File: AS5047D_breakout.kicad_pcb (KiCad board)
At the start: 2 copper layers, 5 parts, among them J1 Conn_01x12_Male, U1 AS5047D

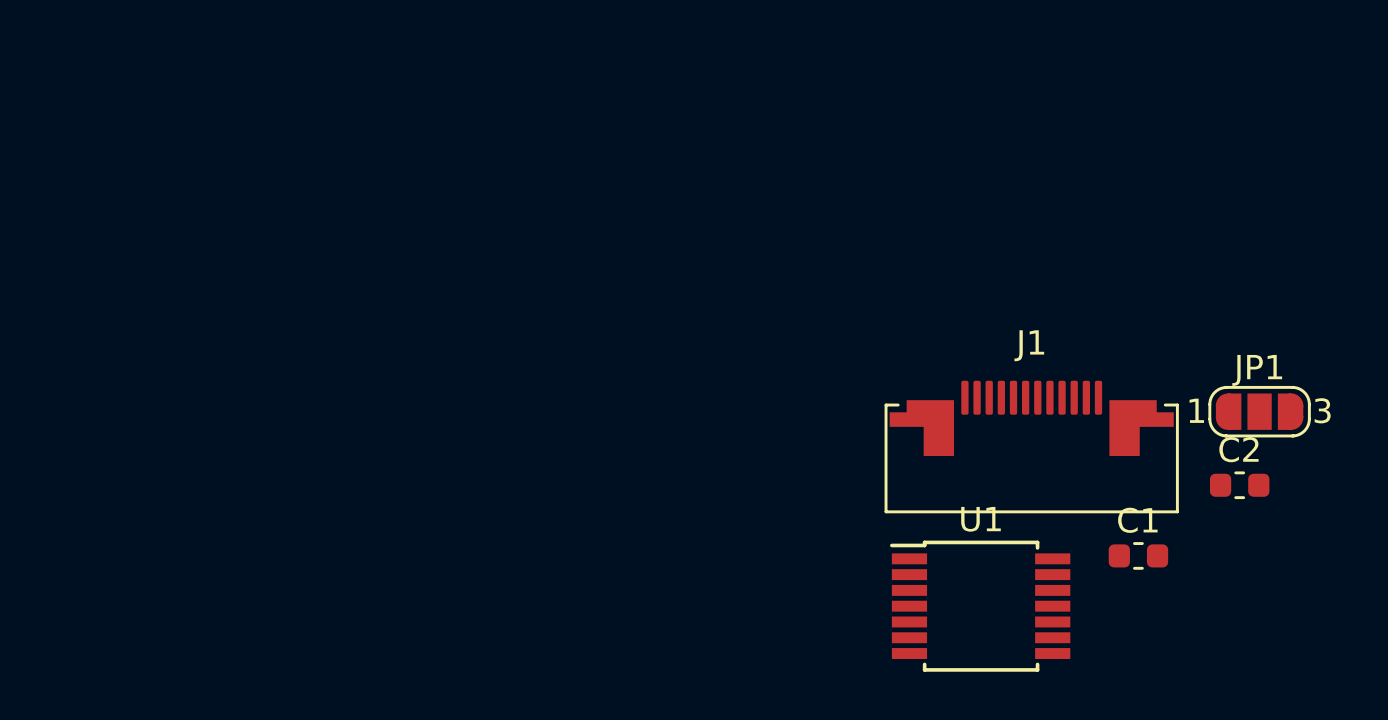
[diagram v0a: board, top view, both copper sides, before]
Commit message: Create encoder breakout board layout
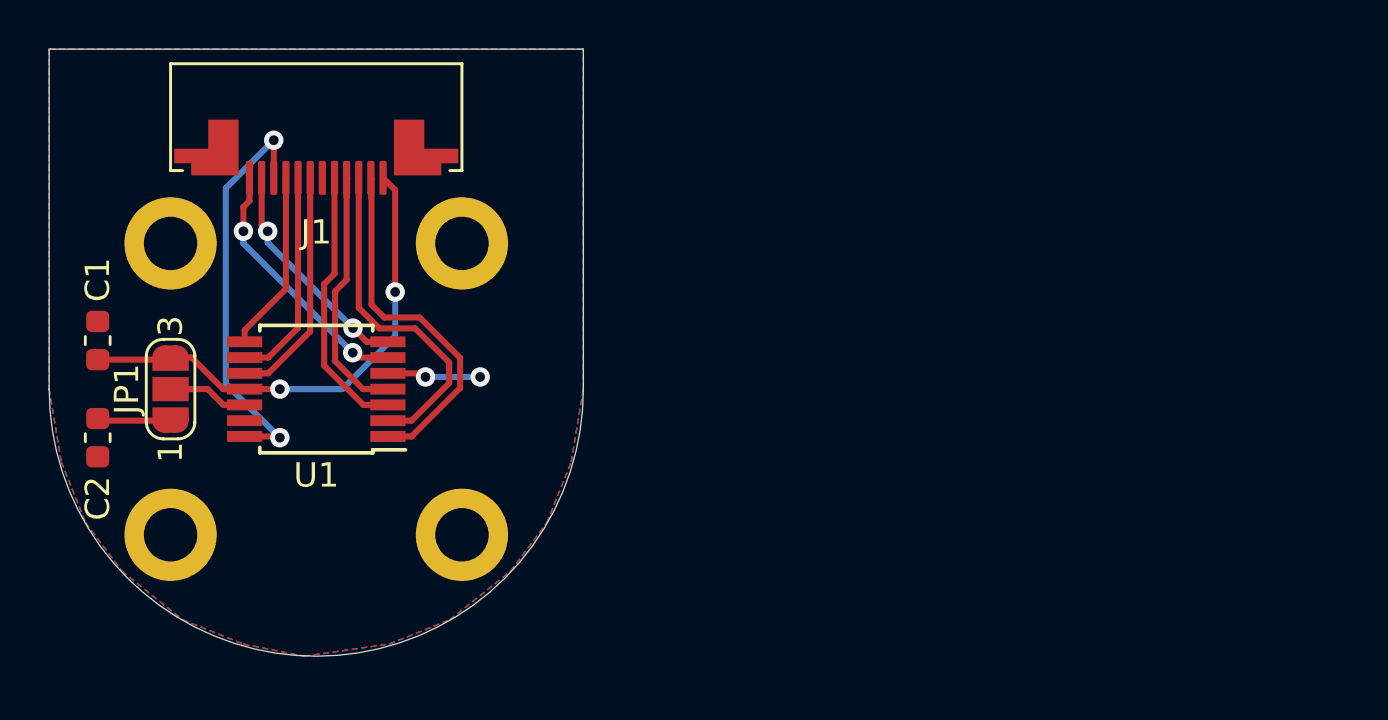
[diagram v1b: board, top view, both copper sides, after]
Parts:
- added G***: LOGO, follow_focus_hw:Gravity_Labs_Logo_Flipped_10mmW, F.Cu at (114.8, 95.8)
- added REF**: MountingHole_2.2mm_M2_DIN965_Pad, MountingHole:MountingHole_2.2mm_M2_DIN965_Pad, F.Cu at (122.0, 102.0)
- added REF**: MountingHole_2.2mm_M2_DIN965_Pad, MountingHole:MountingHole_2.2mm_M2_DIN965_Pad, F.Cu at (110.0, 102.0)
- added REF**: MountingHole_2.2mm_M2_DIN965_Pad, MountingHole:MountingHole_2.2mm_M2_DIN965_Pad, F.Cu at (110.0, 90.0)
- added REF**: MountingHole_2.2mm_M2_DIN965_Pad, MountingHole:MountingHole_2.2mm_M2_DIN965_Pad, F.Cu at (122.0, 90.0)
- moved C2 47.1 mm to (107.0, 98.0), turned to 270 degrees
- moved JP1 44.9 mm to (110.0, 96.0), turned to 90 degrees
- moved C1 43.8 mm to (107.0, 94.0), turned to 90 degrees
- moved J1 31.0 mm to (116.0, 87.0), turned to 180 degrees
- moved U1 28.8 mm to (116.0, 96.0), turned to 180 degrees
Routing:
- net VDD: track 0.00 -> 20.5 mm, vias 0 -> 2
- net /I: track 0.00 -> 17.0 mm, vias 0 -> 2
- net /CSN: track 0.00 -> 15.6 mm
- net /CLK: track 0.00 -> 14.0 mm
- net /MISO: track 0.00 -> 11.2 mm
- net /MOSI: track 0.00 -> 11.2 mm
- net /B: track 0.00 -> 10.7 mm, vias 0 -> 2
- net /U: track 0.00 -> 9.74 mm
- net /A: track 0.00 -> 9.42 mm, vias 0 -> 2
- net /V: track 0.00 -> 8.88 mm
- net /W: track 0.00 -> 7.45 mm
- net GND: track 0.00 -> 3.86 mm, vias 0 -> 2
- net Net-(JP1-Pad2): track 0.00 -> 3.32 mm
- net Net-(C2-Pad1): track 0.00 -> 3.04 mm
- added copper zone on B.Cu, net GND
- added copper zone on F.Cu, net GND
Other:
- board outline added: 22 x 25 mm
- board text added: "Created By: Eduardo Mucino Andrew Chau"

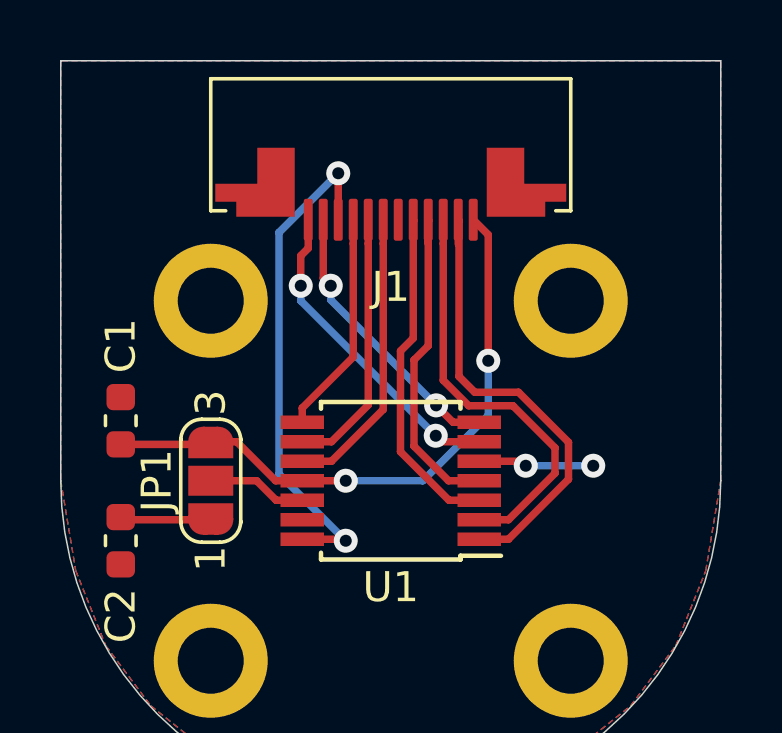
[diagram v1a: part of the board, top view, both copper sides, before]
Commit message: Adjust harness connector location on AS5047D board
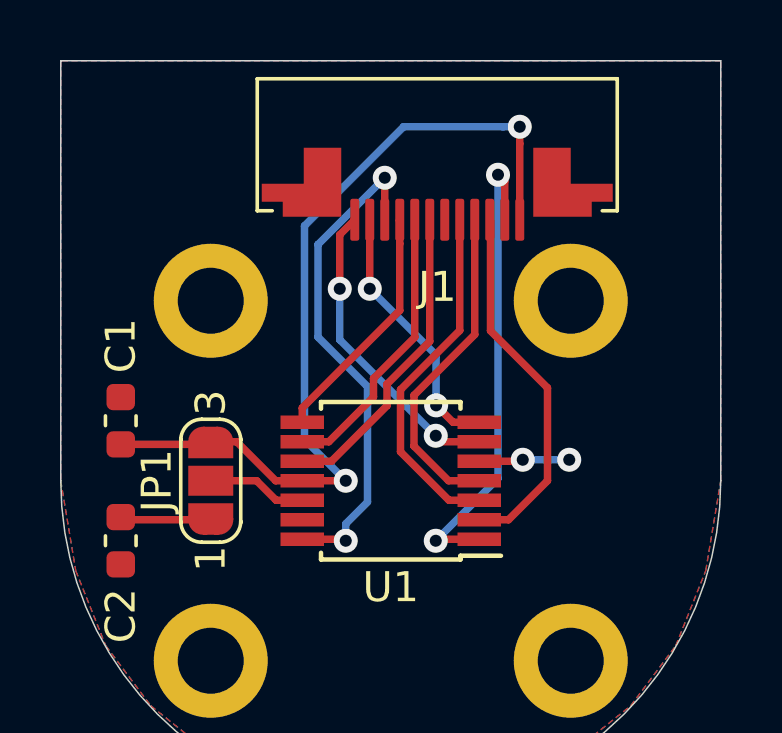
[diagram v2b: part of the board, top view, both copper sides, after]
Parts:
- moved J1 1.55 mm to (117.5, 87.0)
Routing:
- net VDD: track 20.5 -> 28.8 mm
- net /CLK: track 14.0 -> 12.3 mm
- net GND: track 3.86 -> 3.02 mm
- net /W: track 7.45 -> 8.13 mm
- net /A: track 9.42 -> 8.77 mm
- net /U: track 9.74 -> 10.4 mm
- net /MISO: track 11.2 -> 11.8 mm
- net /V: track 8.88 -> 9.47 mm
- net /CSN: track 15.6 -> 16.1 mm, vias 0 -> 2

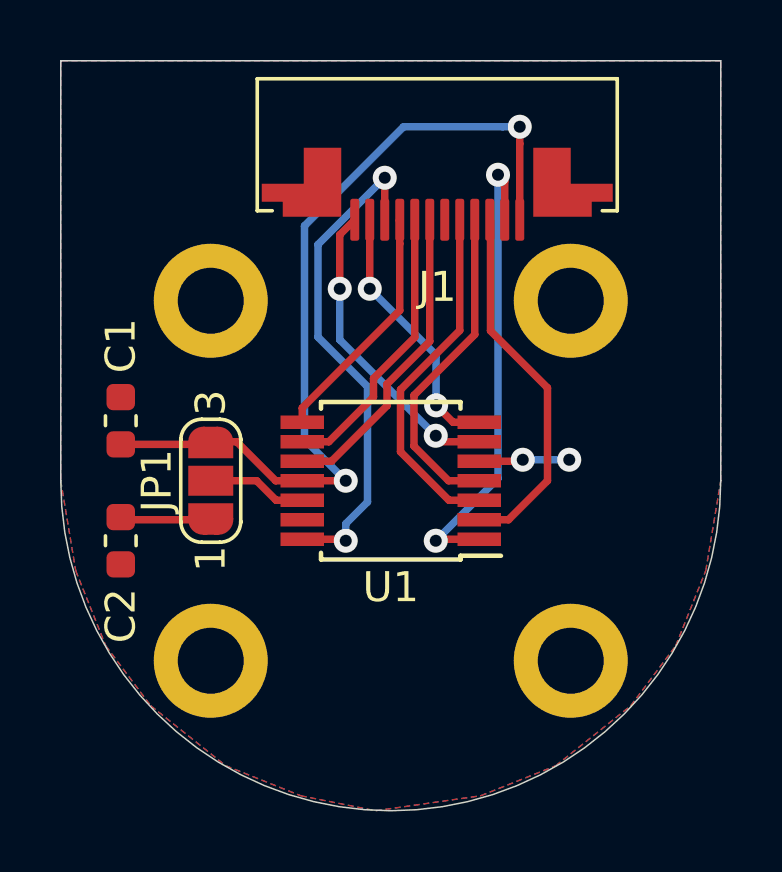
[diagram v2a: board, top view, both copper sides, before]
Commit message: Modify AS5047D breakout form factor
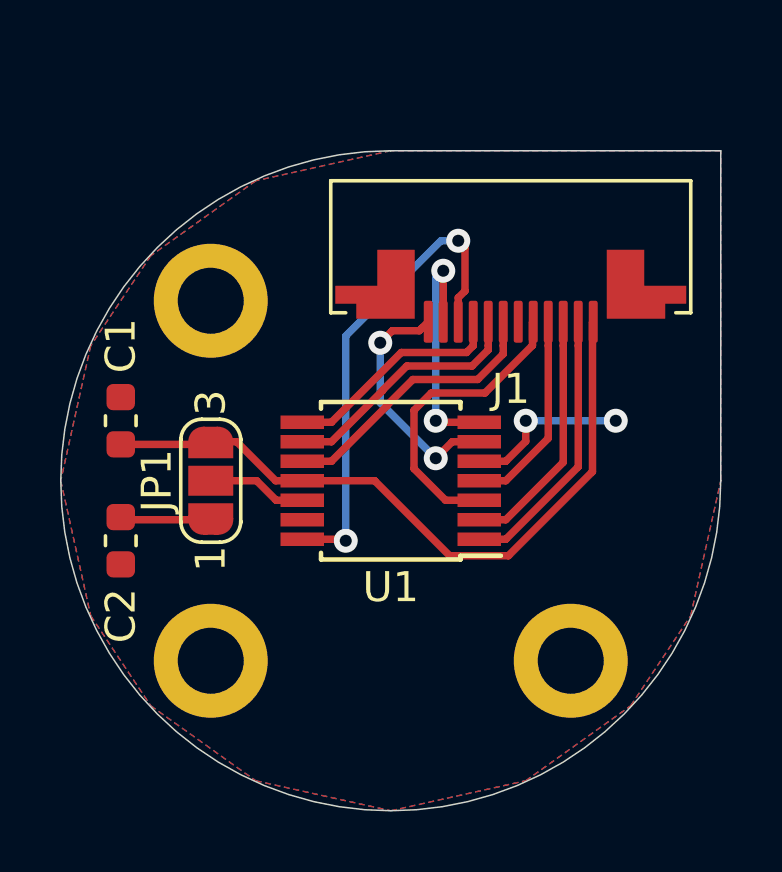
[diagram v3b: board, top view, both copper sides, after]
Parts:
- removed the REF** at (122.0, 90.0)
- moved J1 4.19 mm to (120.0, 90.4)
- moved G*** 0.25 mm to (114.5, 95.8)
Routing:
- net /CSN: track 16.1 -> 9.14 mm, vias 2 -> 0
- net VDD: track 28.8 -> 23.5 mm, vias 2 -> 0
- net /MOSI: track 11.0 -> 6.77 mm
- net /CLK: track 12.3 -> 8.28 mm
- net GND: track 3.02 -> 5.51 mm
- net /B: track 10.3 -> 8.18 mm
- net /MISO: track 11.8 -> 10.2 mm
- net /U: track 10.4 -> 9.26 mm
- net /V: track 9.47 -> 8.41 mm
- net /I: track 16.9 -> 16.2 mm
- net /W: track 8.13 -> 7.56 mm
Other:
- board size 22 x 25 mm -> 22 x 22 mm
